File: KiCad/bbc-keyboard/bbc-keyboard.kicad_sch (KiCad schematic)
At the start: 7 parts

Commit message: schema
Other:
- added sheet muxdemux (muxdemux.kicad_sch)
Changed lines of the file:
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@@
     (pin "1")
+  )
+  (sheet (at 124.46 86.36) (size 36.83 26.67) (fields_autoplaced)
+    (stroke (width 0.1524) (type solid) (color 0 0 0 0))
+    (fill (color 0 0 0 0.0000))
+    (property "Sheet name" "muxdemux" (id 0) (at 124.46 85.6484 0)
+      (effects (font (size 1.27 1.27)) (justify left bottom))
+    )
+    (property "Sheet file" "muxdemux.kicad_sch" (id 1) (at 124.46 113.6146 0)
+      (effects (font (size 1.27 1.27)) (justify left top))
+    )
   )
   (sheet_instances
     (path "/" (page "1"))
+    (path "/6149d2d9-e610-4c07-b8fa-fc11a7f5479e" (page "2"))
   )
   (symbol_instances
+    (path "/6149d2d9-e610-4c07-b8fa-fc11a7f5479e/392bb0ad-f5cf-4ed5-910c-8b55cd3cf9a6"
+      (reference "#PWR?") (unit 1) (value "VCC") (footprint "")
+    )
     (path "/da3bbfd5-7f58-455d-a0a3-e46770be8164"
       (reference "#PWR?") (unit 1) (value "VCC") (footprint "")
@@
       (reference "#PWR?") (unit 1) (value "GND") (footprint "")
     )
+    (path "/6149d2d9-e610-4c07-b8fa-fc11a7f5479e/6a6d7b8b-d246-4418-8cd9-65ca8e377644"
+      (reference "IC1") (unit 1) (value "74LS161") (footprint "")
+    )
     (path "/5414043a-ed38-4cec-828b-be5302069545"

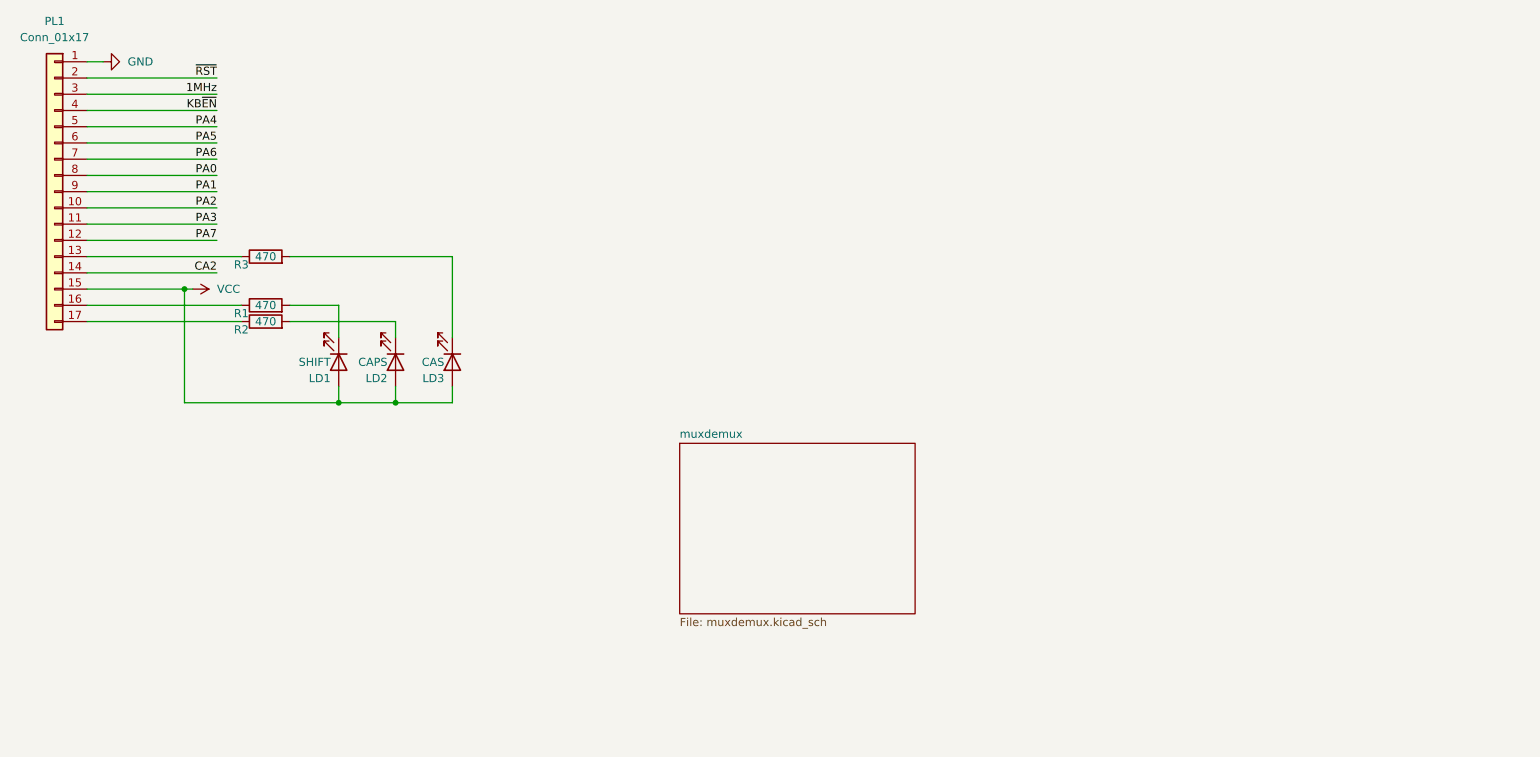
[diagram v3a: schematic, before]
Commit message: Fix up ERC
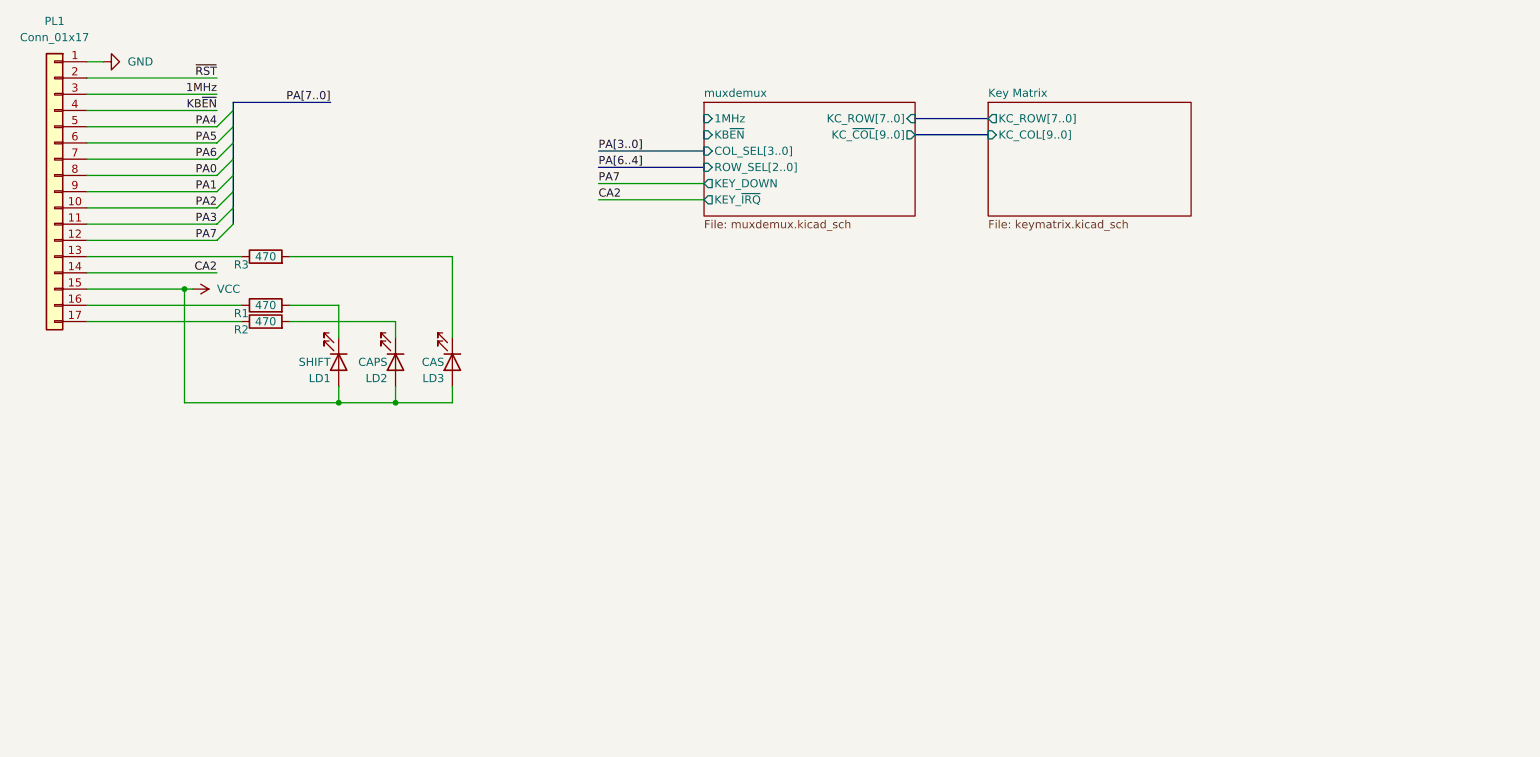
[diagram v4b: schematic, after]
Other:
- added sheet Key Matrix (keymatrix.kicad_sch)
- sheet muxdemux ports: added 1MHz, COL_SEL[3..0], KB~{EN}, KC_ROW[7..0], KC_~{COL}[9..0], KEY_DOWN, KEY_~{IRQ}, ROW_SEL[2..0]; removed none

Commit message: pull ups
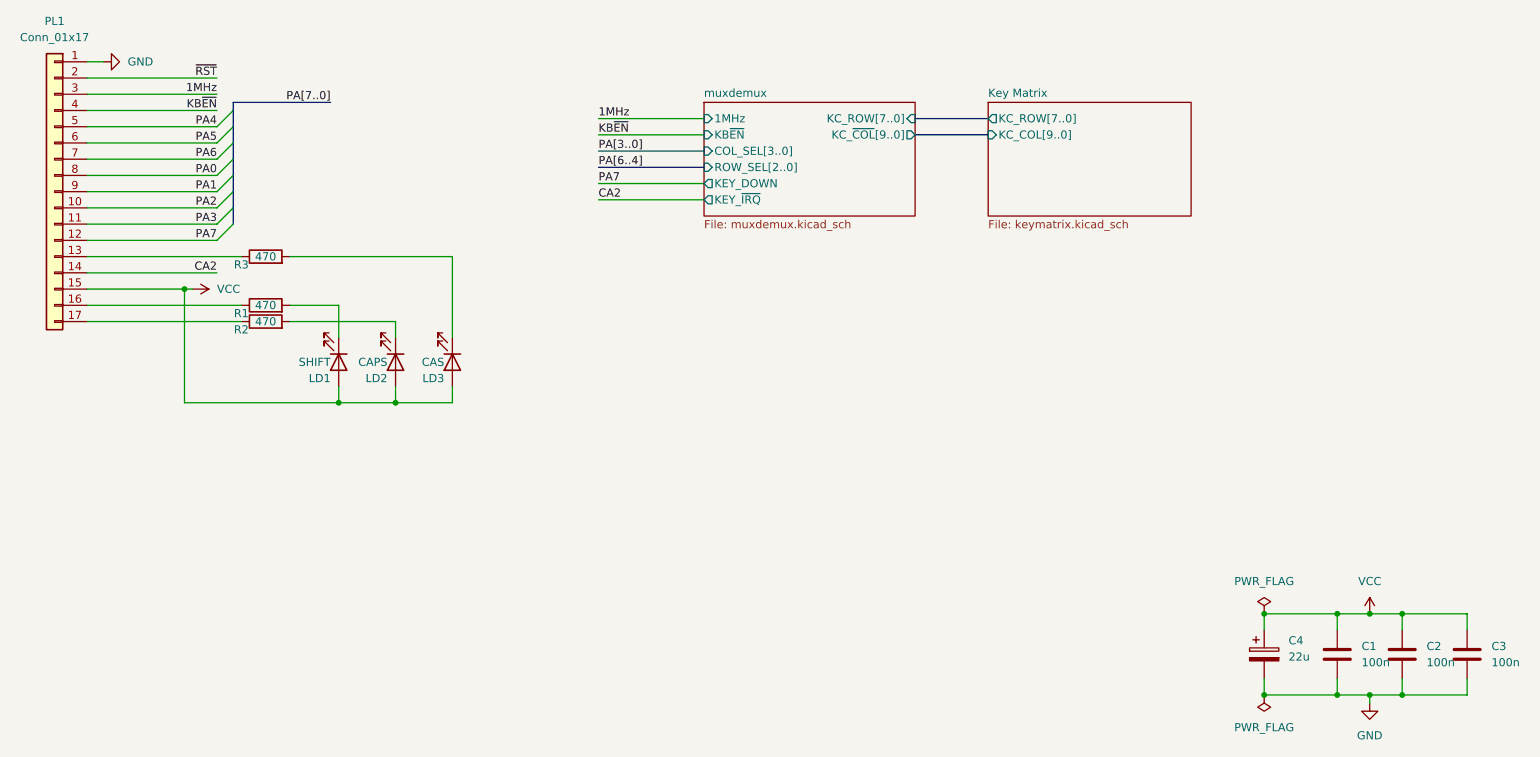
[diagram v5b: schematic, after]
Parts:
- added C1, C2, C3: 100n, symbol Device:C
- added C4: 22u, symbol Device:C_Polarized
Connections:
- net GND: now also C1.2, C2.2, C3.2, C4.2
- net VCC: now also C1.1, C2.1, C3.1, C4.1

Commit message: Break Key
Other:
- sheet Key Matrix ports: added ~{RST}; removed none
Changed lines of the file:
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@@
     (stroke (width 0) (type default) (color 0 0 0 0))
   )
-  (bus (pts (xy 161.29 38.1) (xy 172.72 38.1))
+  (bus (pts (xy 161.29 38.1) (xy 182.88 38.1))
     (stroke (width 0) (type default) (color 0 0 0 0))
   )
@@
     (stroke (width 0) (type default) (color 0 0 0 0))
   )
+  (wire (pts (xy 173.355 47.625) (xy 182.88 47.625))
+    (stroke (width 0) (type default) (color 0 0 0 0))
+  )
   (bus (pts (xy 54.61 44.45) (xy 54.61 41.91))
     (stroke (width 0) (type default) (color 0 0 0 0))
@@
     (stroke (width 0) (type default) (color 0 0 0 0))
   )
-  (bus (pts (xy 161.29 35.56) (xy 172.72 35.56))
+  (bus (pts (xy 161.29 35.56) (xy 182.88 35.56))
     (stroke (width 0) (type default) (color 0 0 0 0))
   )
@@
   )
   (label "PA[3..0]" (at 111.76 40.64 0)
+    (effects (font (size 1.27 1.27)) (justify left bottom))
+  )
+  (label "~{RST}" (at 173.355 47.625 0)
     (effects (font (size 1.27 1.27)) (justify left bottom))
   )
@@
     (pin "1")
   )
-  (sheet (at 172.72 33.02) (size 31.75 17.78) (fields_autoplaced)
+  (sheet (at 182.88 33.02) (size 31.75 17.78) (fields_autoplaced)
     (stroke (width 0.1524) (type solid) (color 0 0 0 0))
     (fill (color 0 0 0 0.0000))
-    (property "Sheet name" "Key Matrix" (id 0) (at 172.72 32.3084 0)
+    (property "Sheet name" "Key Matrix" (id 0) (at 182.88 32.3084 0)
       (effects (font (size 1.27 1.27)) (justify left bottom))
     )
-    (property "Sheet file" "keymatrix.kicad_sch" (id 1) (at 172.72 51.3846 0)
+    (property "Sheet file" "keymatrix.kicad_sch" (id 1) (at 182.88 51.3846 0)
       (effects (font (size 1.27 1.27)) (justify left top))
     )
-    (pin "KC_COL[9..0]" input (at 172.72 38.1 180)
-      (effects (font (size 1.27 1.27)) (justify left))
-    )
-    (pin "KC_ROW[7..0]" output (at 172.72 35.56 180)
+    (pin "KC_COL[9..0]" input (at 182.88 38.1 180)
+      (effects (font (size 1.27 1.27)) (justify left))
+    )
+    (pin "KC_ROW[7..0]" output (at 182.88 35.56 180)
+      (effects (font (size 1.27 1.27)) (justify left))
+    )
+    (pin "~{RST}" output (at 182.88 47.625 180)
       (effects (font (size 1.27 1.27)) (justify left))
     )
@@
       (reference "#PWR0109") (unit 1) (value "VCC") (footprint "")
     )
+    (path "/5a6afae0-4df7-4603-b305-1b33d5f2e402/7eea0b84-bfae-436e-8694-1a79a65d6c74"
+      (reference "#PWR?") (unit 1) (value "GND") (footprint "")
+    )
     (path "/1999562b-3aa3-4942-8f9a-0c18378bf41e"
       (reference "C1") (unit 1) (value "100n") (footprint "")
@@
       (reference "SW74") (unit 1) (value "SW_DIP_x08") (footprint "")
     )
-  )
+    (path "/5a6afae0-4df7-4603-b305-1b33d5f2e402/53f914f1-d751-4149-8cd9-30532b860fe7"
+      (reference "SW?") (unit 1) (value "break") (footprint "")
+    )
+  )
